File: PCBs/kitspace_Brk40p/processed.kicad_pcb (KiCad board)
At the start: 2 copper layers, 53.1 x 51.8 mm, 6 parts, among them J1 Conn_01x40, J2 Conn_01x40_MountingPin

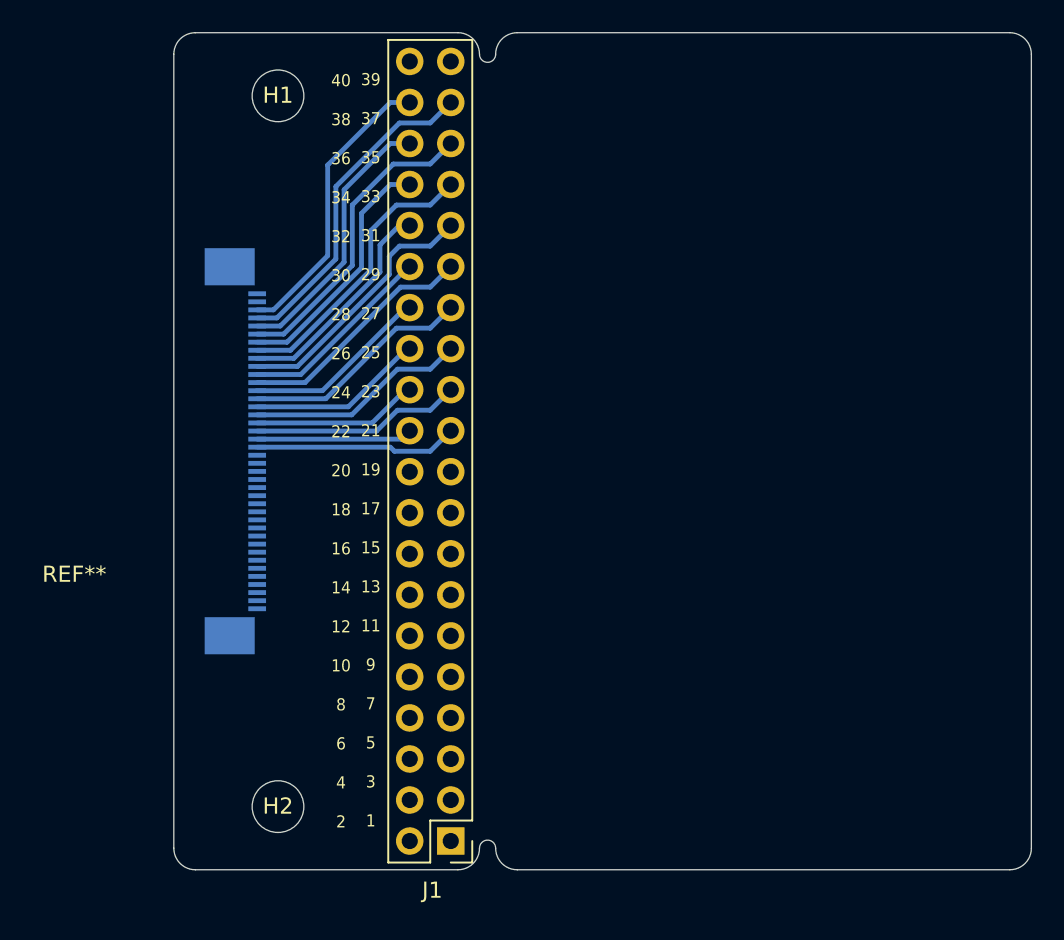
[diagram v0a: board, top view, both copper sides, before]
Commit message: recheck all circuits and clean up fill zone by rerouting the nets using freerouting and manually
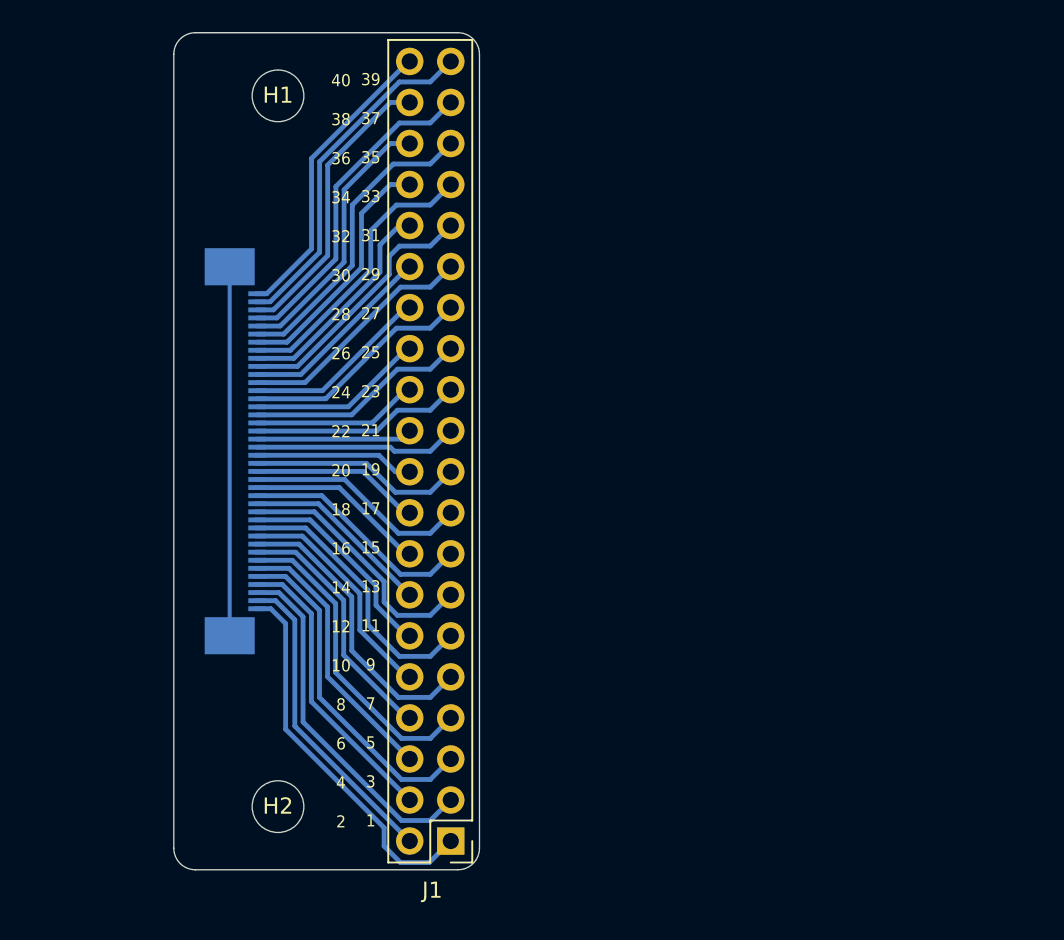
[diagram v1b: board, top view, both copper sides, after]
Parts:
- removed REF**: SolderWire-0.1sqmm_1x01_D0.4mm_OD1mm, Connector_Wire:SolderWire-0.1sqmm_1x01_D0.4mm_OD1mm
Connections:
- J1 pad 1: (no net) -> Net-(J1-Pad1)
- J1 pad 10: (no net) -> Net-(J1-Pad10)
- J1 pad 11: (no net) -> Net-(J1-Pad11)
- J1 pad 12: (no net) -> Net-(J1-Pad12)
- J1 pad 13: (no net) -> Net-(J1-Pad13)
- J1 pad 14: (no net) -> Net-(J1-Pad14)
- J1 pad 15: (no net) -> Net-(J1-Pad15)
- J1 pad 16: (no net) -> Net-(J1-Pad16)
- J1 pad 17: (no net) -> Net-(J1-Pad17)
- J1 pad 18: (no net) -> Net-(J1-Pad18)
- J1 pad 19: (no net) -> Net-(J1-Pad19)
- J1 pad 2: (no net) -> Net-(J1-Pad2)
- J1 pad 20: (no net) -> Net-(J1-Pad20)
- J1 pad 3: (no net) -> Net-(J1-Pad3)
- J1 pad 39: (no net) -> Net-(J1-Pad39)
- J1 pad 4: (no net) -> Net-(J1-Pad4)
- J1 pad 40: (no net) -> Net-(J1-Pad40)
- J1 pad 5: (no net) -> Net-(J1-Pad5)
- J1 pad 6: (no net) -> Net-(J1-Pad6)
- J1 pad 7: (no net) -> Net-(J1-Pad7)
- J1 pad 8: (no net) -> Net-(J1-Pad8)
- J1 pad 9: (no net) -> Net-(J1-Pad9)
- J2 pad 1: (no net) -> Net-(J1-Pad1)
- J2 pad 10: (no net) -> Net-(J1-Pad10)
- J2 pad 11: (no net) -> Net-(J1-Pad11)
- J2 pad 12: (no net) -> Net-(J1-Pad12)
- J2 pad 13: (no net) -> Net-(J1-Pad13)
- J2 pad 14: (no net) -> Net-(J1-Pad14)
- J2 pad 15: (no net) -> Net-(J1-Pad15)
- J2 pad 16: (no net) -> Net-(J1-Pad16)
- J2 pad 17: (no net) -> Net-(J1-Pad17)
- J2 pad 18: (no net) -> Net-(J1-Pad18)
- J2 pad 19: (no net) -> Net-(J1-Pad19)
- J2 pad 2: (no net) -> Net-(J1-Pad2)
- J2 pad 20: (no net) -> Net-(J1-Pad20)
- J2 pad 3: (no net) -> Net-(J1-Pad3)
- J2 pad 39: (no net) -> Net-(J1-Pad39)
- J2 pad 4: (no net) -> Net-(J1-Pad4)
- J2 pad 40: (no net) -> Net-(J1-Pad40)
- J2 pad 5: (no net) -> Net-(J1-Pad5)
- J2 pad 6: (no net) -> Net-(J1-Pad6)
- J2 pad 7: (no net) -> Net-(J1-Pad7)
- J2 pad 8: (no net) -> Net-(J1-Pad8)
- J2 pad 9: (no net) -> Net-(J1-Pad9)
- J2 pad MP: (no net) -> GND
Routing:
- net Net-(J1-Pad1): track 0.00 -> 23.7 mm
- net GND: track 0.00 -> 22.8 mm
- net Net-(J1-Pad3): track 0.00 -> 22.3 mm
- net Net-(J1-Pad39): track 0.00 -> 21.6 mm
- net Net-(J1-Pad5): track 0.00 -> 21.0 mm
- net Net-(J1-Pad7): track 0.00 -> 19.7 mm
- net Net-(J1-Pad2): track 0.00 -> 19.6 mm
- net Net-(J1-Pad40): track 0.00 -> 18.8 mm
- net Net-(J1-Pad9): track 0.00 -> 18.5 mm
- net Net-(J1-Pad4): track 0.00 -> 18.3 mm
- net Net-(J1-Pad11): track 0.00 -> 17.2 mm
- net Net-(J1-Pad6): track 0.00 -> 17.0 mm
- net Net-(J1-Pad13): track 0.00 -> 16.0 mm
- net Net-(J1-Pad8): track 0.00 -> 15.8 mm
- net Net-(J1-Pad15): track 0.00 -> 14.7 mm
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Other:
- board size 53.1 x 51.8 mm -> 18.9 x 51.8 mm

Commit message: clean psbc that are missed before
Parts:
- gave numbers to parts that had none: 1
